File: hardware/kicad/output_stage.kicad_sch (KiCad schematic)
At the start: 18 parts, among them J801 VOUT, Q801 CSD17577Q3A, Q802 CSD17577Q3A, U801 OPA197IDBV

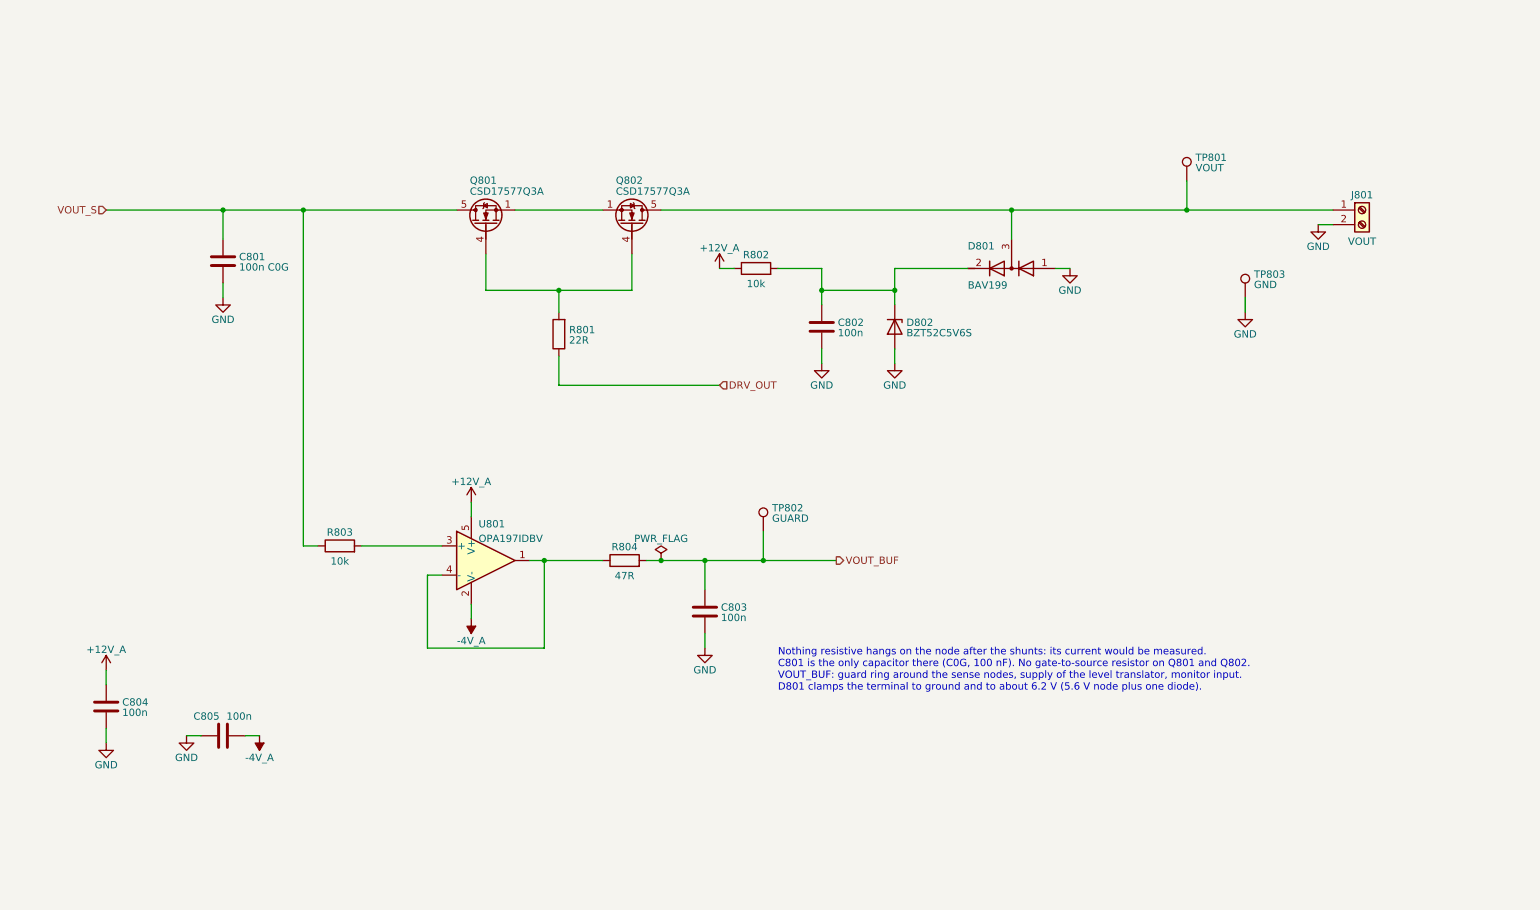
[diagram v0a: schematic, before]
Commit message: feat(hardware)!: draw draft A1 of the schematic around a Pico 2
A Raspberry Pi Pico 2 on two 1x20 sockets replaces the ESP32-S3
development board, the programmable logic device and the buffer
between the two boards (D-39 to D-43 of the specification). The former
interface and range logic sheets become two new ones:

- Controller: the Pico 2, the diodes that join its USB supply and the
  5 V rail of the carrier, resistor arrays in the SPI and acquisition
  lines, a reset button and a console header.
- Side Data: two shift registers that take the range, the status
  signals and the eight logic inputs with every sample.

The DUT connects through a 1x4 pin header and a lever terminal block
in parallel, both GND, VIN, VOUT, GND, and the logic port is a 1x10
header with VCC, GND, D7 to D0: the pin order of the PPK2 (D-44). A
solder jumper selects the supply of the DUT side of the level
translator. A transistor at the driver of the ampere switch holds it
open while VIN is above 5.5 V.

Reference designators are numbered as the annotation tool of KiCad
does by default (D-45). The numbering touches every sheet, so these
changes come in one commit. The symbol and the socket footprint of
the ESP32-S3 board leave the project library; the Pico 2 uses the
symbol and the footprint of the KiCad library.

The electrical rules check reports no errors and no warnings. The
parts stay candidates, and no program for the PIO blocks exists yet.

BREAKING CHANGE: the pins of the controller follow the new pin map of
section 5 of the specification.
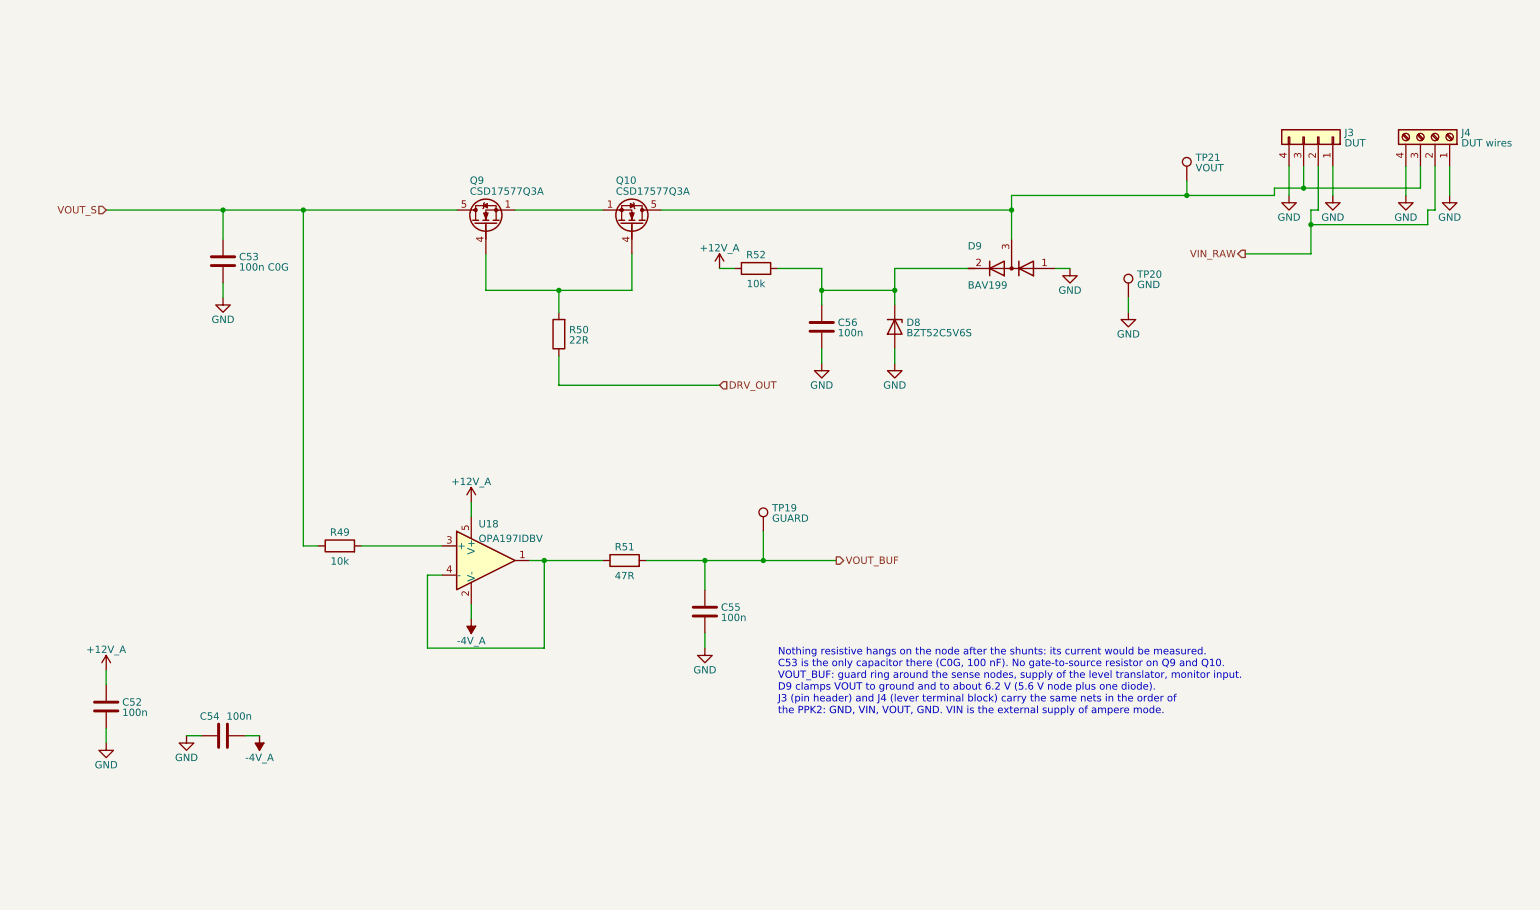
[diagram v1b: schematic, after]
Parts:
- added J4: DUT wires, TerminalBlock_WAGO:TerminalBlock_WAGO_2601-1104_1x04_P3.50mm_Horizontal, symbol Connector:Screw_Terminal_01x04
- J3: renamed from J801; value VOUT -> DUT; footprint TerminalBlock_Phoenix:TerminalBlock_Phoenix_MKDS-1,5-2-5.08_1x02_P5.08mm_Horizontal -> Connector_PinHeader_2.54mm:PinHeader_1x04_P2.54mm_Vertical; symbol Connector:Screw_Terminal_01x02 -> Connector_Generic:Conn_01x04; Note (none) -> 2.54 mm pin header, straight or angled: GND, VIN, VOUT, GND
- renumbered C804 to C52, C801 to C53, C805 to C54, C803 to C55, C802 to C56, D802 to D8, D801 to D9, Q802 to Q10, Q801 to Q9, R803 to R49, R801 to R50, R804 to R51, R802 to R52, TP802 to TP19, TP803 to TP20, TP801 to TP21, U801 to U18
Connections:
- net GND: now also J3.1 (Pin_1), J3.4 (Pin_4), J4.1 (Pin_1), J4.4 (Pin_4); no longer J3.2 (Pin_2)
- net at D9.3 (common), Q10.5 (D), TP21.1: now also J3.3 (Pin_3), J4.3 (Pin_3); no longer J3.1 (Pin_1)
- new net VIN_RAW: J3.2 (Pin_2), J4.2 (Pin_2)
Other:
- note added: "Nothing resistive hangs on the node after the shunts: its current would be measured. C53 is the only capacitor there (C0G, 100 nF). No gate-to-source resistor on Q9 and Q10. VOUT_BUF: guard ring around the sense nodes, supply of the level translator, monitor input. D9 clamps VOUT to ground and to about 6.2 V (5.6 V node plus one diode). J3 (pin header) and J4 (lever terminal block) carry the same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"
- note removed: "Nothing resistive hangs on the node after the shunts: its current would be measured. C801 is the only capacitor there (C0G, 100 nF). No gate-to-source resistor on Q801 and Q802. VOUT_BUF: guard ring around the sense nodes, supply of the level translator, monitor input. D801 clamps the terminal to ground and to about 6.2 V (5.6 V node plus one diode)."
- title: Output Switch, VOUT Terminal and Guard Buffer -> Output Switch, DUT Connectors and Guard Buffer
- moved on the sheet: TP20

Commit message: feat(hardware): draw draft A2 of the schematic
428 parts on 15 A4 pages, 14 sheets below the root sheet (D-83). Two
sheets are new: Logic Supplies, with the supervisor of the 5 V rail and
the two 3.3 V regulators, and Rail Monitor, with the comparators behind
PWR_GOOD.

The drawings follow the specification of draft A2: a current limiter
on each supply input and a priority multiplexer, a pre-regulator that
tracks the output of the linear regulator, a VIN path that withstands
-20 V to +20 V with its switch open, two diode-connected MOSFETs as
ladder clamp, thin-film and four-terminal shunts, ESD arrays at the CC
pins and at the VCC pin of the logic port. The reference designators
are numbered as KiCad numbers them (D-45), so they are not those of
draft A1.

The project library gains the symbol of the input multiplexer and two
footprints: the lever terminal block with pads of 1.9 mm x 2.3 mm and
the controller module without its antenna keep-out (D-85).

The electrical rules check reports no errors and no warnings. The
parts are candidates, and nothing is built or measured.
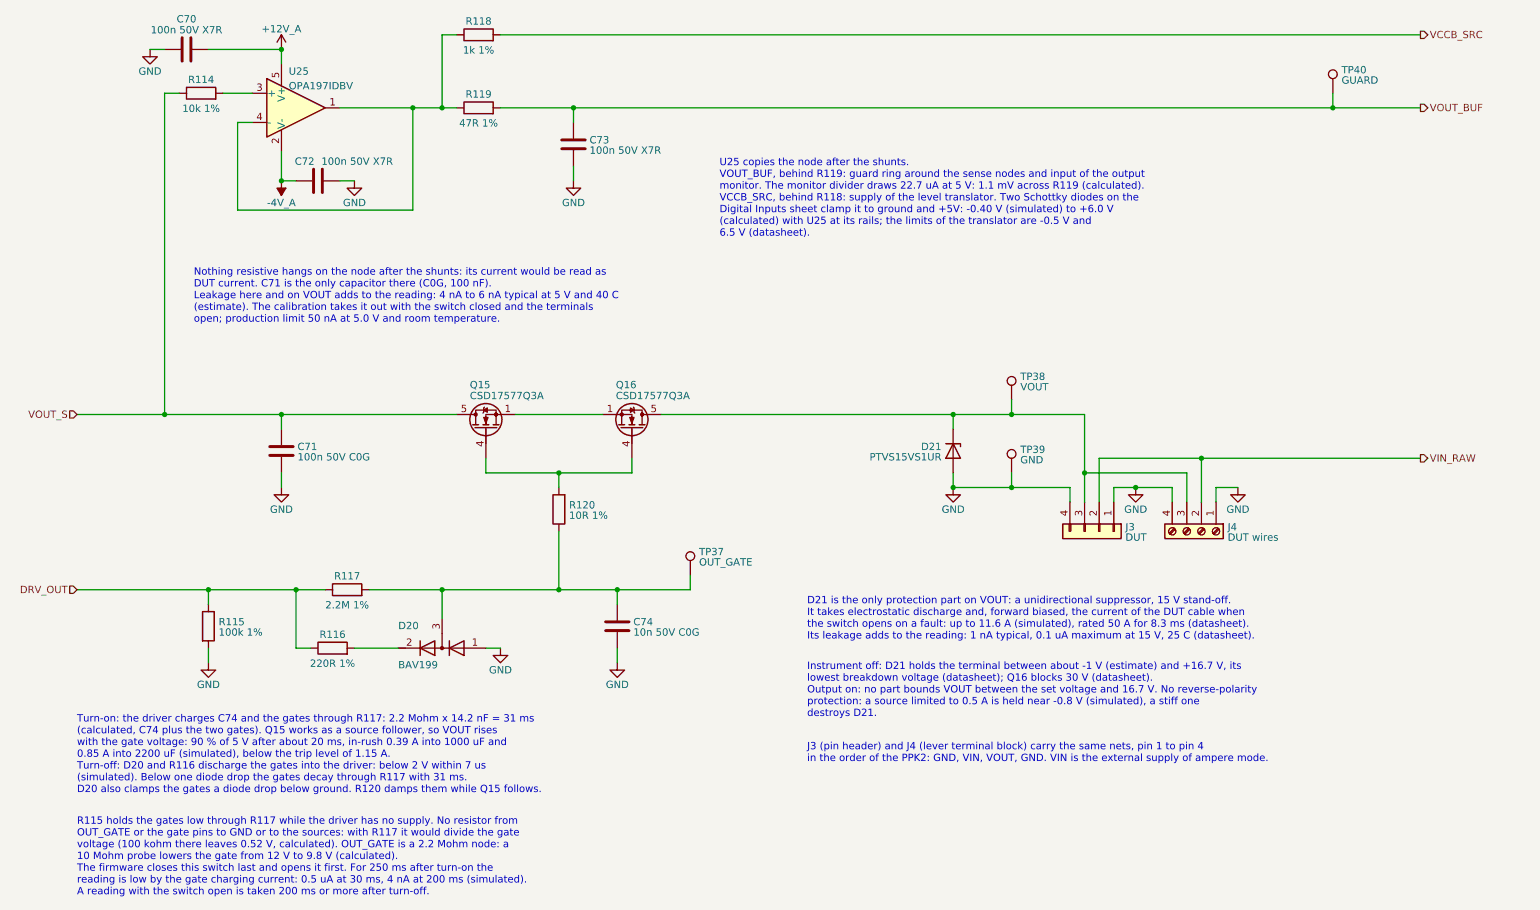
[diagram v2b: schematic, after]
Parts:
- removed C56: 100n, Capacitor_SMD:C_0603_1608Metric, symbol Device:C
- removed D8: BZT52C5V6S, Diode_SMD:D_SOD-323, symbol Device:D_Zener
- removed R52: 10k, Resistor_SMD:R_0603_1608Metric, symbol Device:R
- added C74: 10n 50V C0G, Capacitor_SMD:C_0603_1608Metric, symbol Device:C
- added D21: PTVS15VS1UR, Diode_SMD:Nexperia_CFP3_SOD-123W, symbol Device:D_Zener
- added R115: 100k 1%, Resistor_SMD:R_0603_1608Metric, symbol Device:R
- added R117: 2.2M 1%, Resistor_SMD:R_0603_1608Metric, symbol Device:R
- added R118: 1k 1%, Resistor_SMD:R_0603_1608Metric, symbol Device:R
- added R120: 10R 1%, Resistor_SMD:R_0603_1608Metric, symbol Device:R
- added TP37: OUT_GATE, TestPoint:TestPoint_Pad_D1.5mm, symbol Connector:TestPoint
- C70: renamed from C52; value 100n -> 100n 50V X7R; MPN (none) -> C0603C104K5RACTU; Manufacturer (none) -> KEMET
- C71: renamed from C53; value 100n C0G -> 100n 50V C0G; MPN (none) -> C3216C0G1H104J160AA; Manufacturer (none) -> TDK
- C72: renamed from C54; value 100n -> 100n 50V X7R; MPN (none) -> C0603C104K5RACTU; Manufacturer (none) -> KEMET
- C73: renamed from C55; value 100n -> 100n 50V X7R; MPN (none) -> C0603C104K5RACTU; Manufacturer (none) -> KEMET
- D20: renamed from D9; MPN (none) -> BAV199-7-F; Manufacturer (none) -> Diodes Incorporated
- J3: MPN (none) -> 61300411121; Manufacturer (none) -> Wurth Elektronik; Note 2.54 mm pin header, straight or angled: GND, VIN, VOUT, GND -> 2.54 mm pin header, straight: GND, VIN, VOUT, GND
- J4: footprint TerminalBlock_WAGO:TerminalBlock_WAGO_2601-1104_1x04_P3.50mm_Horizontal -> PowerProfiler:TerminalBlock_WAGO_2601-1104_1x04_P3.50mm_Horizontal_Pad1.9mm; Manufacturer (none) -> WAGO
- Q15: renamed from Q9; MPN (none) -> CSD17577Q3A; Manufacturer (none) -> Texas Instruments
- Q16: renamed from Q10; MPN (none) -> CSD17577Q3A; Manufacturer (none) -> Texas Instruments
- R114: renamed from R49; value 10k -> 10k 1%; MPN (none) -> CRCW060310K0FKEA; Manufacturer (none) -> Vishay
- R116: renamed from R50; value 22R -> 220R 1%; MPN (none) -> CRCW0603220RFKEA; Manufacturer (none) -> Vishay
- R119: renamed from R51; value 47R -> 47R 1%; MPN (none) -> CRCW060347R0FKEA; Manufacturer (none) -> Vishay
- TP38: renamed from TP21; now left out of the parts list
- TP39: renamed from TP20; now left out of the parts list
- TP40: renamed from TP19; now left out of the parts list
- U25: renamed from U18; MPN (none) -> OPA197IDBVR; Manufacturer (none) -> Texas Instruments
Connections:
- net DRV_OUT: now also R115.1, R117.1
- net GND: now also C74.2, D21.2 (A), R115.2
- net at D20.2 (K): now also R116.2
- net at J3.3 (Pin_3), J4.3 (Pin_3), Q16.5 (D)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: now also D21.1 (K); no longer D20.3 (common)
- net at R119.1, U25.1, U25.4 (-): now also R118.1
- net at Q15.4 (G), Q16.4 (G): now also R120.2; no longer R116.2
- new net: C74.1, D20.3 (common), R117.2, R120.1, TP37.1
- new net VCCB_SRC: R118.2
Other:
- note added: "D21 is the only protection part on VOUT: a unidirectional suppressor, 15 V stand-off. It takes electrostatic discharge and, forward biased, the current of the DUT cable when the switch opens on a fault: up to 11.6 A (simulated), rated 50 A for 8.3 ms (datasheet). Its leakage adds to the reading: 1 nA typical, 0.1 uA maximum at 15 V, 25 C (datasheet)."
- note added: "Instrument off: D21 holds the terminal between about -1 V (estimate) and +16.7 V, its lowest breakdown voltage (datasheet); Q16 blocks 30 V (datasheet). Output on: no part bounds VOUT between the set voltage and 16.7 V. No reverse-polarity protection: a source limited to 0.5 A is held near -0.8 V (simulated), a stiff one destroys D21."
- note added: "J3 (pin header) and J4 (lever terminal block) carry the same nets, pin 1 to pin 4 in the order of the PPK2: GND, VIN, VOUT, GND. VIN is the external supply of ampere mode."
- note added: "Nothing resistive hangs on the node after the shunts: its current would be read as DUT current. C71 is the only capacitor there (C0G, 100 nF). Leakage here and on VOUT adds to the reading: 4 nA to 6 nA typical at 5 V and 40 C (estimate). The calibration takes it out with the switch closed and the terminals open; production limit 50 nA at 5.0 V and room temperature."
- note added: "R115 holds the gates low through R117 while the driver has no supply. No resistor from OUT_GATE or the gate pins to GND or to the sources: with R117 it would divide the gate voltage (100 kohm there leaves 0.52 V, calculated). OUT_GATE is a 2.2 Mohm node: a 10 Mohm probe lowers the gate from 12 V to 9.8 V (calculated). The firmware closes this switch last and opens it first. For 250 ms after turn-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"
- note added: "Turn-on: the driver charges C74 and the gates through R117: 2.2 Mohm x 14.2 nF = 31 ms (calculated, C74 plus the two gates). Q15 works as a source follower, so VOUT rises with the gate voltage: 90 % of 5 V after about 20 ms, in-rush 0.39 A into 1000 uF and 0.85 A into 2200 uF (simulated), below the trip level of 1.15 A. Turn-off: D20 and R116 discharge the gates into the driver: below 2 V within 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"
- note added: "U25 copies the node after the shunts. VOUT_BUF, behind R119: guard ring around the sense nodes and input of the output monitor. The monitor divider draws 22.7 uA at 5 V: 1.1 mV across R119 (calculated). VCCB_SRC, behind R118: supply of the level translator. Two Schottky diodes on the Digital Inputs sheet clamp it to ground and +5V: -0.40 V (simulated) to +6.0 V (calculated) with U25 at its rails;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"
- note removed: "Nothing resistive hangs on the node after the shunts: its current would be measured. C53 is the only capacitor there (C0G, 100 nF). No gate-to-source resistor on Q9 and Q10. VOUT_BUF: guard ring around the sense nodes, supply of the level translator, monitor input. D9 clamps VOUT to ground and to about 6.2 V (5.6 V node plus one diode). J3 (pin header) and J4 (lever terminal block) carry the same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"
- moved on the sheet: C70, C71, C72, C73, D20, J3, J4, Q15, Q16, R114, R116, R119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
